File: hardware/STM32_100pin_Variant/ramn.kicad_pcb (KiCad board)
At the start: 2 copper layers, 93.6 x 70 mm, 140 parts, among them J1 USB_C_Micro, J2 Screw_Terminal_01x03, J3 , J4 , J5 , J6 , U1 STM32L4S7VITx, U10 STM32L4S7VITx, U11 ATA6561-GAQW-N, U12 NCV8163, U2 ATA6561-GAQW-N, U3 NCV8163, U4 STM32L4S7VITx, U5 ATA6561-GAQW-N, U6 NCV8163, U7 STM32L4S7VITx, U8 ATA6561-GAQW-N, U9 NCV8163, Y1 Crystal_GND24, Y2 Crystal_GND24, Y3 Crystal_GND24, Y4 Crystal_GND24

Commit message: Generated Gerber Files
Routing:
- net GND: track 781.3 -> 776.1 mm, vias 65 -> 62
- net /ECUD/X2: track 7.13 -> 5.92 mm
- net /ECUD/X1: track 18.3 -> 17.1 mm
- net /ECUC/3V3_ECU: track 117.2 -> 116.1 mm
- net /usb_uc/3V3_ECU: track 115.8 -> 114.8 mm
- net +5V: track 350.7 -> 349.8 mm
- net Net-(C1-Pad1): track 20.4 -> 19.5 mm
- net /ECUB/X2: track 5.40 -> 4.60 mm
- net /ECUB/X1: track 8.11 -> 7.32 mm
- net /ECUC/PA4: track 15.4 -> 14.7 mm
- net /ECUC/X1: track 9.81 -> 9.10 mm
- net /ECUB/PB13: track 15.7 -> 15.0 mm
- net /ECUD/PB0: track 8.91 -> 8.22 mm
- net /usb_uc/X2: track 7.20 -> 6.53 mm
- net /usb_uc/PB11: track 8.91 -> 8.28 mm
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
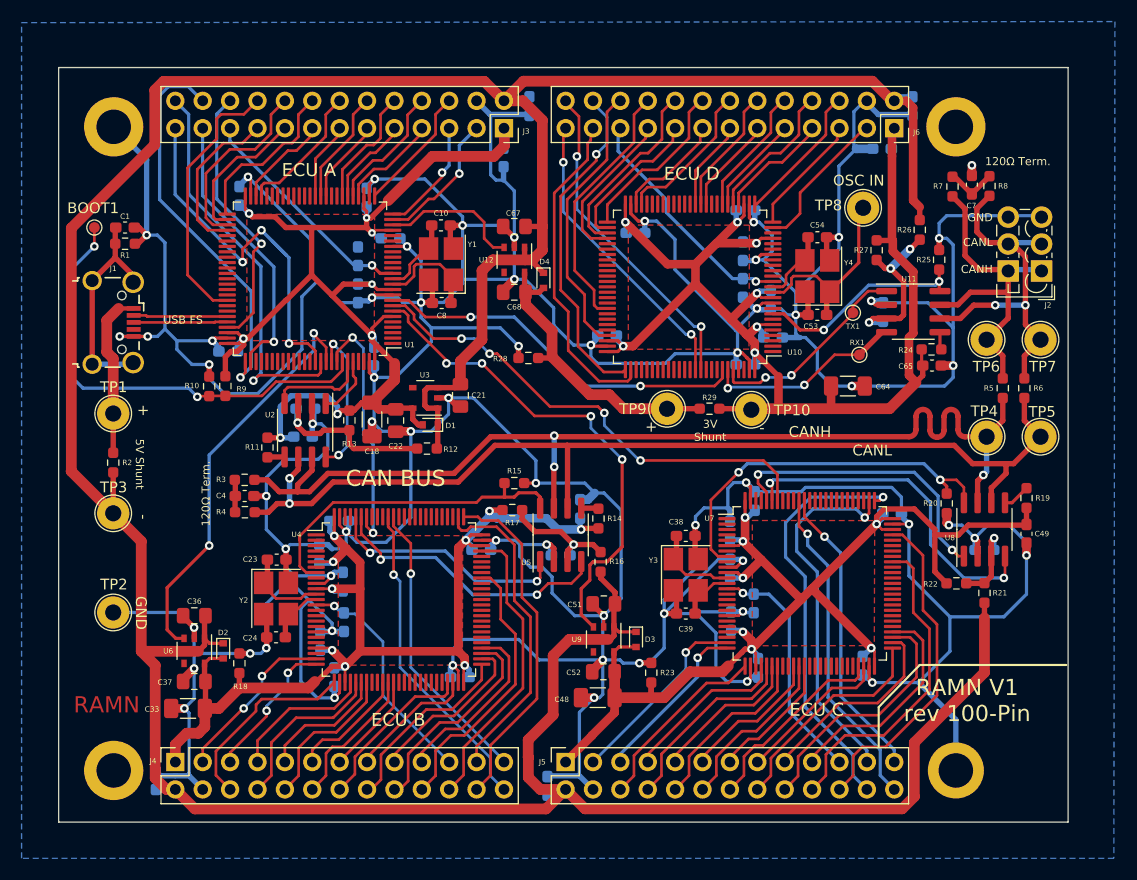
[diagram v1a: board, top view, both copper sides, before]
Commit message: Removed OSC_IN Test Point
Test point removed to prevent - --increased capacitance and noise on the high-frequency crystal oscillator line. Can hook up oscilloscope directly to crystal's capacitor when needed.
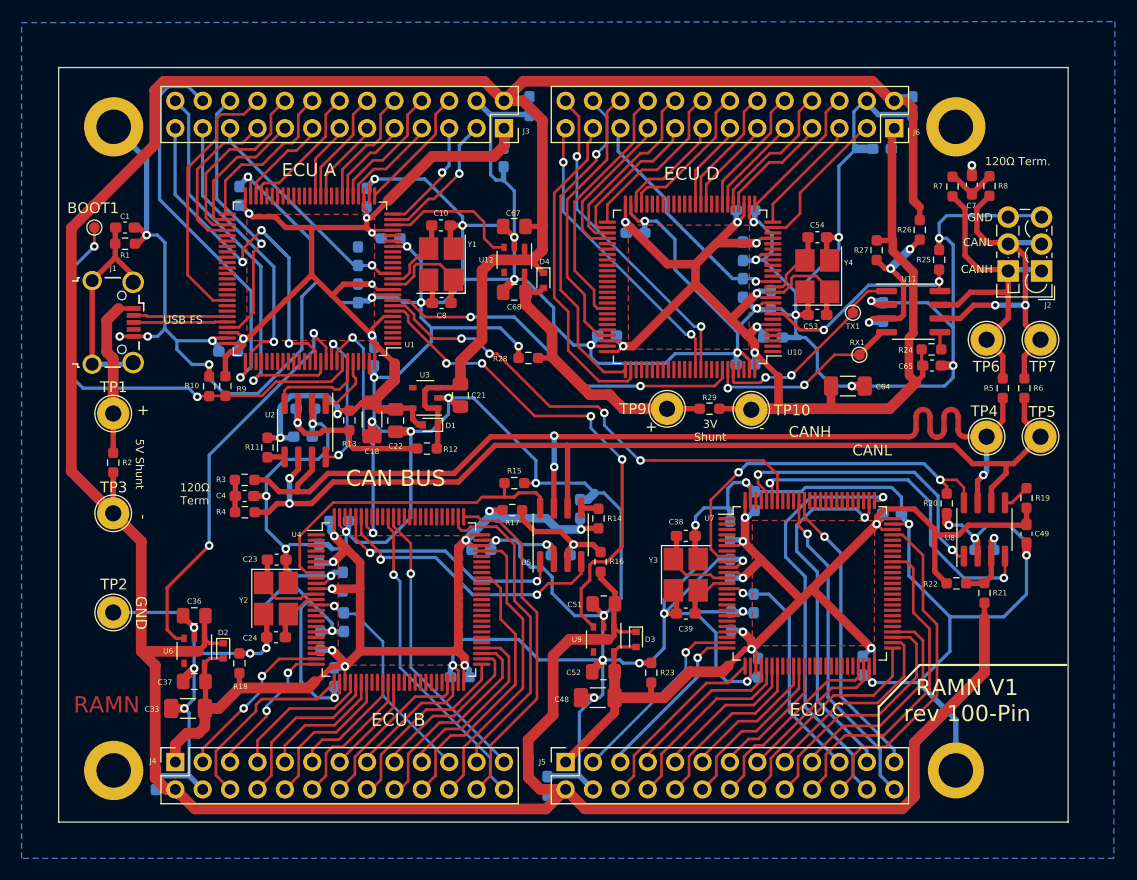
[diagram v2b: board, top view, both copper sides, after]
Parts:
- removed TP8: , TestPoint:TestPoint_Loop_D2.54mm_Drill1.5mm_Beaded
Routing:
- net /ECUD/X1: track 17.1 -> 8.63 mm
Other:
- board text added: "120Ω Term"
- board text removed: "OSC IN"
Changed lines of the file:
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@@
   )
   (footprint "TestPoint:TestPoint_Loop_D2.54mm_Drill1.5mm_Beaded" (layer "F.Cu")
-    (at 113.95 54.5)
-    (descr "wire loop with bead as test point, loop diameter2.548mm, hole diameter 1.5mm")
-    (tags "test point wire loop bead")
-    (property "Sheetfile" "sc_uc.kicad_sch")
-    (property "Sheetname" "ECUD")
-    (attr through_hole)
-    (fp_text reference "TP8" (at -3.21 -0.23) (layer "F.SilkS")
-      (effects (font (size 1 1) (thickness 0.15)))
-    )
-    (fp_text value " " (at 0 -2.8) (layer "F.Fab")
-      (effects (font (size 1 1) (thickness 0.15)))
-    )
-    (fp_text user "${REFERENCE}" (at 0.7 2.5) (layer "F.Fab")
-      (effects (font (size 1 1) (thickness 0.15)))
-    )
-    (fp_circle (center 0 0) (end 1.7 0) (layer "F.SilkS") (width 0.12) (fill none))
-    (fp_circle (center 0 0) (end 2 0) (layer "F.CrtYd") (width 0.05) (fill none))
-    (fp_line (start -1.3 0.3) (end 1.3 0.3) (layer "F.Fab") (width 0.12))
-    (fp_line (start 1.3 0.3) (end 1.3 -0.3) (layer "F.Fab") (width 0.12))
-    (fp_line (start 1.3 -0.3) (end -1.3 -0.3) (layer "F.Fab") (width 0.12))
-    (fp_line (start -1.3 -0.3) (end -1.3 0.3) (layer "F.Fab") (width 0.12))
-    (fp_circle (center 0 0) (end 1.5 0) (layer "F.Fab") (width 0.12) (fill none))
-    (pad "1" thru_hole circle (at 0 0) (size 3 3) (drill 1.5) (layers *.Cu *.Mask)
-      (net 368 "/ECUD/X1") (pinfunction "1") (pintype "passive"))
-    (model "${KICAD6_3DMODEL_DIR}/TestPoint.3dshapes/TestPoint_Loop_D2.54mm_Drill1.5mm_Beaded.wrl"
-      (offset (xyz 0 0 0))
-      (scale (xyz 1 1 1))
-      (rotate (xyz 0 0 0))
-    )
-  )
-  (footprint "TestPoint:TestPoint_Loop_D2.54mm_Drill1.5mm_Beaded" (layer "F.Cu")
     (at 130.405 75.73)
     (descr "wire loop with bead as test point, loop diameter2.548mm, hole diameter 1.5mm")
@@
   (gr_line (start 119.2 96.9) (end 132.8 96.9) (layer "F.SilkS") (width 0.2))
   (gr_line (start 115.4 100.8) (end 119.2 96.9) (layer "F.SilkS") (width 0.2))
-  (gr_line (start 115.4 104.5) (end 115.4 100.8) (layer "F.SilkS") (width 0.2))
+  (gr_line (start 115.4 104.394) (end 115.4 100.694) (layer "F.SilkS") (width 0.2))
   (gr_rect (start 39.35 41.49) (end 132.962883 111.47) (layer "Edge.Cuts") (width 0.05) (fill none))
   (gr_text "RAMN" (at 43.8 100.6) (layer "F.Cu")
@@
     (effects (font (size 1.5 1.5) (thickness 0.3)))
   )
-  (gr_text "OSC IN" (at 113.55 51.97) (layer "F.SilkS")
-    (effects (font (size 1 1) (thickness 0.2)))
-  )
   (gr_text "+" (at 47.18 73.26) (layer "F.SilkS")
     (effects (font (size 1 1) (thickness 0.15)))
@@
     (effects (font (size 0.75 0.75) (thickness 0.15)))
   )
-  (gr_text "120Ω Term." (at 53 81 90) (layer "F.SilkS")
+  (gr_text "120Ω\nTerm" (at 51.9684 81.0514) (layer "F.SilkS")
     (effects (font (size 0.75 0.75) (thickness 0.15)))
   )
@@
   (segment (start 107.505 60.83) (end 109.605 60.83) (width 0.25) (layer "F.Cu") (net 368))
   (segment (start 106.605 62.33) (end 107.305 61.63) (width 0.25) (layer "F.Cu") (net 368))
-  (segment (start 113.55 54.9) (end 113.55 59.585) (width 0.3) (layer "F.Cu") (net 368))
-  (segment (start 113.55 59.585) (end 110.855 62.28) (width 0.3) (layer "F.Cu") (net 368))
   (segment (start 106.505 61.83) (end 105.58 61.83) (width 0.25) (layer "F.Cu") (net 369))
   (segment (start 106.805 60.73) (end 106.805 61.53) (width 0.25) (layer "F.Cu") (net 369))
